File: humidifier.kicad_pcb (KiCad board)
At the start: 2 copper layers, 39 x 24 mm, 12 parts, among them J1 Level, J2 PWR, Q1 IRF740, U1 NE555

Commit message: Release candidate.
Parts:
- added D1: 4141, Diode_THT:D_DO-15_P3.81mm_Vertical_AnodeUp, B.Cu at (101.2, 88.0)
- added J3: FAN, Connector_Wire:SolderWirePad_1x02_P7.62mm_Drill2mm, F.Cu at (107.2, 100.0)
- added Q2: 13001, Package_TO_SOT_THT:TO-92, B.Cu at (96.2, 88.0)
- added R1: 1k, Resistor_SMD:R_0805_2012Metric_Pad1.15x1.40mm_HandSolder, F.Cu at (93.2, 93.0)
- RV1: footprint Connector_PinSocket_2.54mm:PinSocket_1x03_P2.54mm_Vertical -> Potentiometer_THT:Potentiometer_Bourns_3386P_Vertical
- moved Q1 127.7 mm to (71.2, 96.0), turned to 90 degrees
- moved C3 122.3 mm to (77.0, 86.2)
- moved J1 122.3 mm to (65.5, 103.0)
- moved L1 122.3 mm to (65.5, 95.5)
- moved R4 122.1 mm to (77.2, 97.0), turned to 180 degrees
- moved BZ1 121.9 mm to (82.2, 87.8)
- moved J2 119.9 mm to (100.2, 100.0)
- moved C1 118.7 mm to (91.7, 96.5)
- moved R3 118.7 mm to (87.5, 93.1)
- moved U1 118.7 mm to (87.4, 104.0)
- moved C2 118.7 mm to (91.2, 99.4)
- moved RV1 115.9 mm to (80.2, 98.0)
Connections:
- net Net-(J1-Pad2) renamed water
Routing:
- net Net-(D1-Pad1): track 0.00 -> 43.5 mm
- net VCC: track 56.2 -> 68.9 mm
- net 26: track 14.1 -> 26.7 mm
- net water: track 17.4 -> 29.3 mm
- net GND: track 59.9 -> 66.2 mm
- net Net-(Q2-Pad3): track 0.00 -> 5.22 mm
- net Net-(C3-Pad2): track 18.5 -> 14.5 mm
- net Net-(Q1-Pad1): track 3.11 -> 5.97 mm
- net Net-(BZ1-Pad1): track 5.16 -> 5.91 mm
- added copper zone on F.Cu, net VCC
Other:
- board size 39 x 24 mm -> 50 x 25 mm
- board text added: "+"
- board text added: "-"
- board text added: "BZ"
- board text added: "GND"
- board text added: "HUM-1.1"
- board text added: "L1"
- board text added: "fan"
- board text added: "vcc"
- board text added: "water"

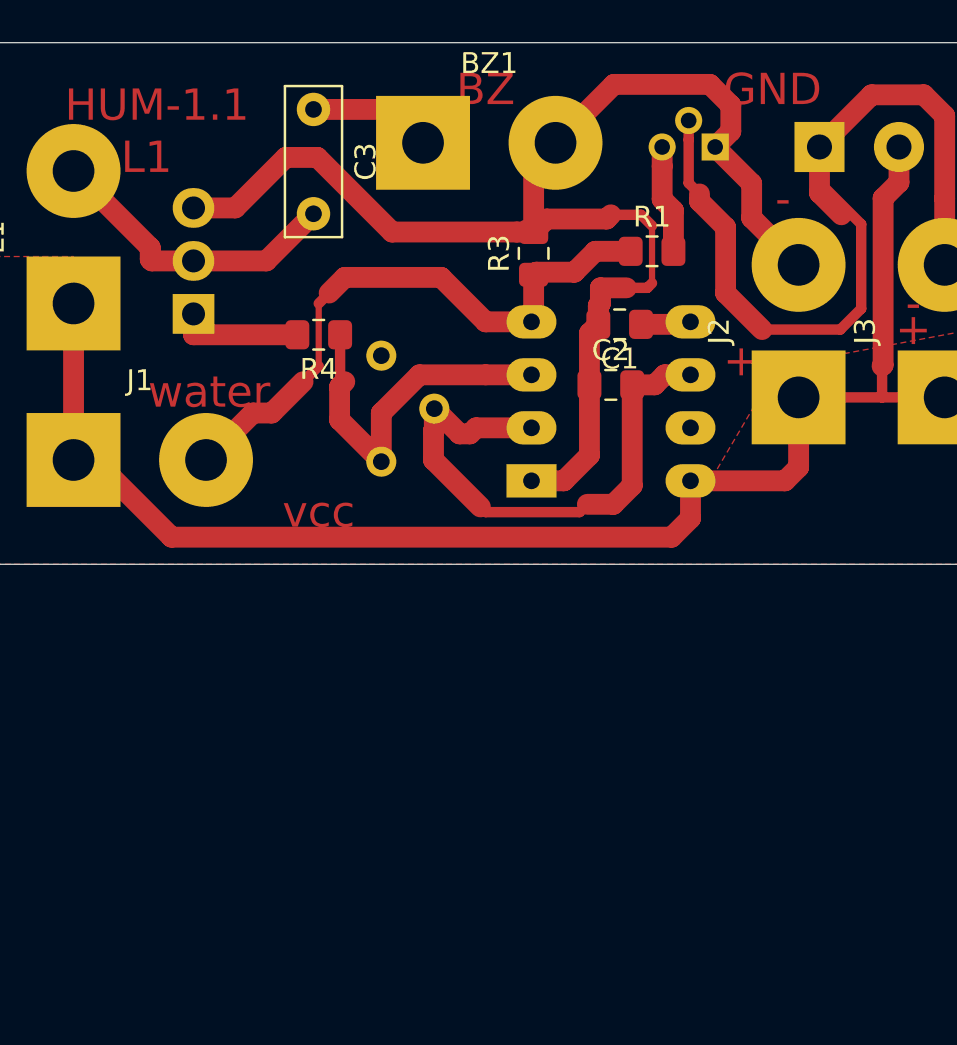
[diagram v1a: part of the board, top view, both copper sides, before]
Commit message: Added sensor based on OA lm324.
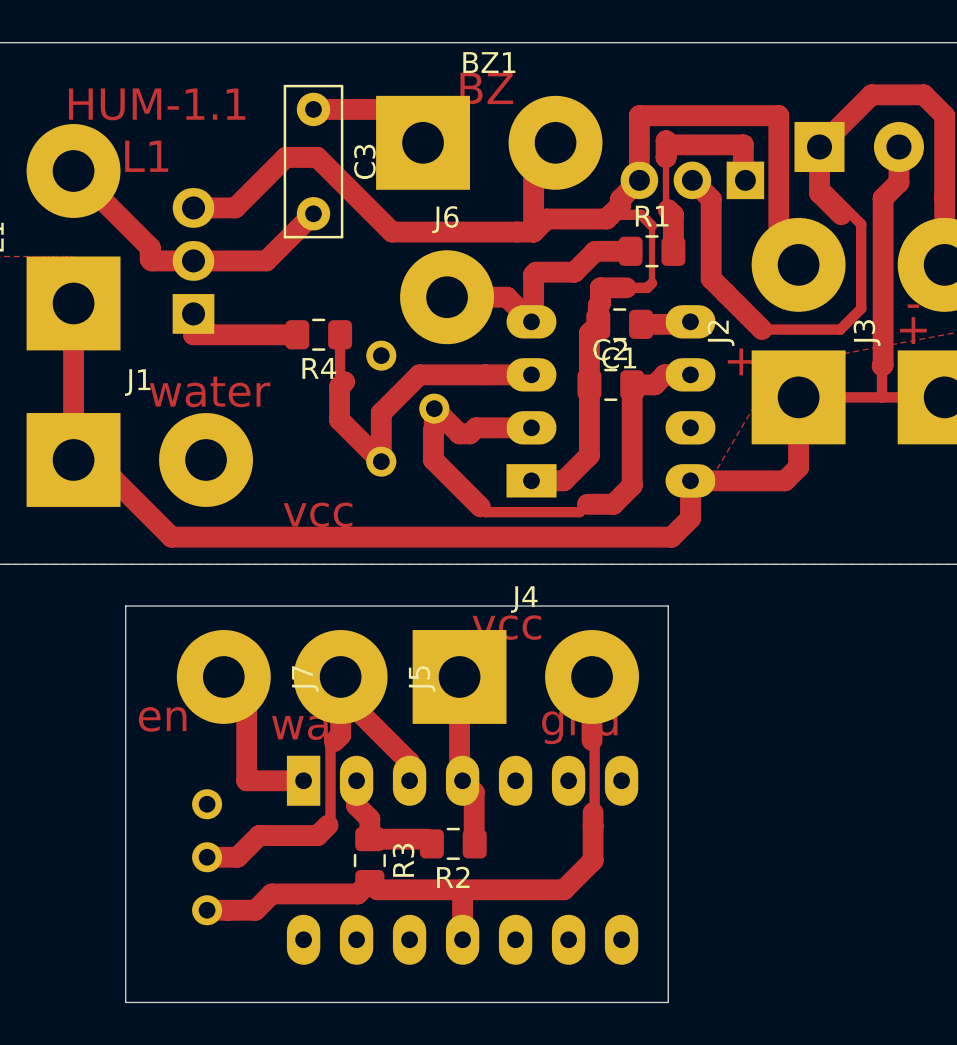
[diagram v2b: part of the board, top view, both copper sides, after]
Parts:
- added J4: PWR, Connector_Wire:SolderWirePad_1x02_P7.62mm_Drill2mm, F.Cu at (84.0, 113.4)
- added J5: water, Connector_Wire:SolderWirePad_1x01_Drill2mm, F.Cu at (78.3, 113.4)
- added J6: en, Connector_Wire:SolderWirePad_1x01_Drill2mm, F.Cu at (83.4, 95.2)
- added J7: en, Connector_Wire:SolderWirePad_1x01_Drill2mm, F.Cu at (72.7, 113.4)
- added R2: 47k, Resistor_SMD:R_0805_2012Metric_Pad1.15x1.40mm_HandSolder, F.Cu at (83.7, 121.4)
- added RV2: 100K, Potentiometer_THT:Potentiometer_Bourns_3296W_Vertical, B.Cu at (71.9, 119.5)
- added U2: LM324, Package_DIP:DIP-14_W7.62mm_LongPads, B.Cu at (76.5, 118.4)
- Q2: value 13001 -> MJE13003; footprint Package_TO_SOT_THT:TO-92 -> Package_TO_SOT_THT:TO-126-3_Vertical
- R3: value 1K -> 47K
- moved R3 30.1 mm to (79.7, 122.2), turned to 270 degrees
- moved Q2 2.16 mm to (97.7, 89.6)
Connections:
- Q2 pad 1: GND -> Net-(Q2-Pad1)
- Q2 pad 3: Net-(Q2-Pad3) -> GND
- R1 pad 1: water -> EN
- R1 pad 2: Net-(Q2-Pad3) -> Net-(Q2-Pad1)
- R3 pad 1: water -> Net-(R2-Pad2)
- U1 pad 4: water -> EN
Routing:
- net GND: track 66.2 -> 98.0 mm
- net EN: track 0.00 -> 20.1 mm
- net Net-(Q2-Pad1): track 0.00 -> 11.0 mm
- net VCC: track 68.9 -> 77.2 mm
- net water: track 29.3 -> 22.2 mm
- net Net-(R2-Pad2): track 0.00 -> 6.13 mm
- net Net-(Q2-Pad3): track 5.22 -> 0.00 mm
- net Net-(D1-Pad1): track 43.5 -> 40.6 mm
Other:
- board size 50 x 25 mm -> 50 x 46 mm
- board text added: "en"
- board text added: "gnd"
- board text added: "wa"
- board text removed: "GND"

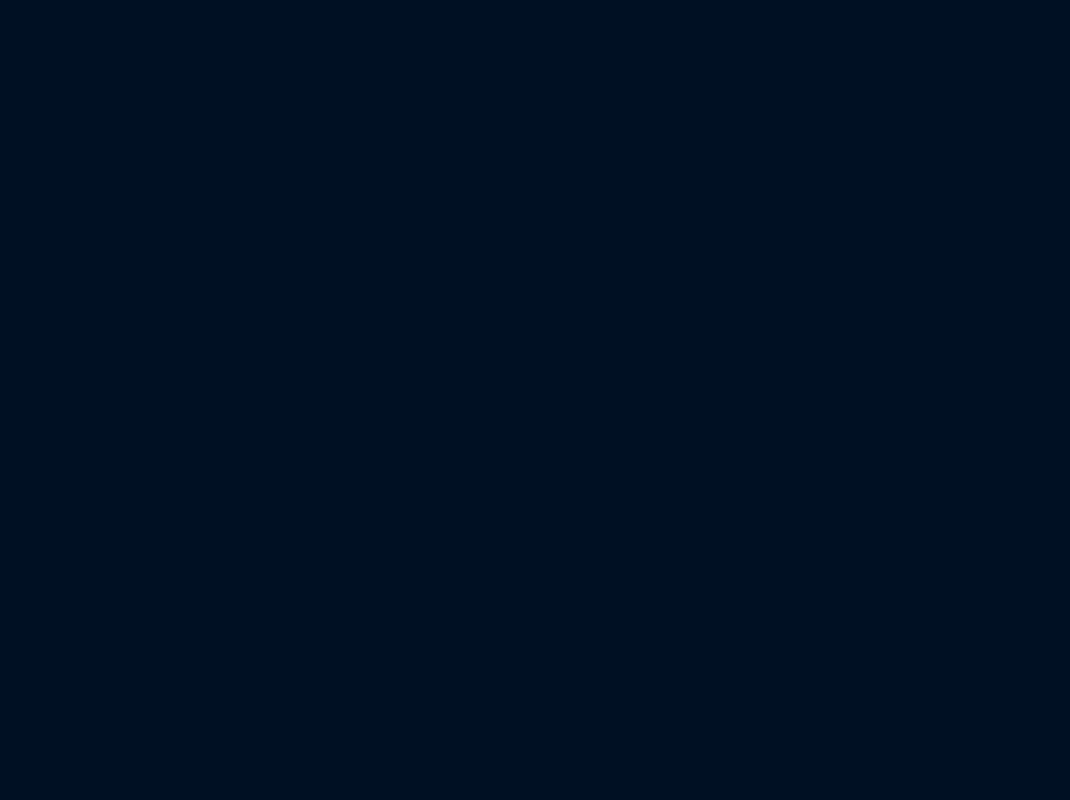
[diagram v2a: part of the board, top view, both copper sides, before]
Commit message: Added timer.
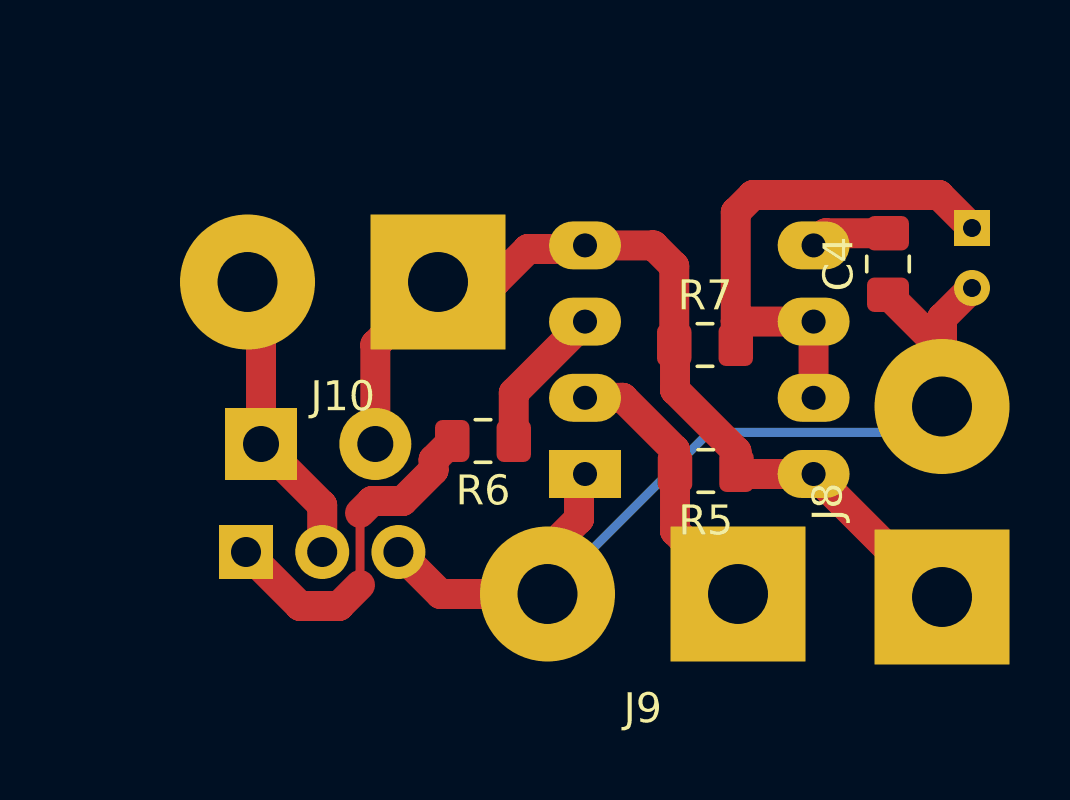
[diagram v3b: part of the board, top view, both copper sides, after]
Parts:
- added C4: 100n, Capacitor_SMD:C_0805_2012Metric_Pad1.15x1.40mm_HandSolder, F.Cu at (124.4, 119.4)
- added C5: 10u, Capacitor_THT:CP_Radial_D4.0mm_P2.00mm, B.Cu at (127.2, 118.2)
- added D2: 4141, Diode_THT:D_DO-15_P3.81mm_Vertical_AnodeUp, B.Cu at (103.5, 125.4)
- added J10: REL, Connector_Wire:SolderWirePad_1x02_P7.62mm_Drill2mm, F.Cu at (109.4, 120.0)
- added J8: PWR, Connector_Wire:SolderWirePad_1x02_P7.62mm_Drill2mm, F.Cu at (126.2, 130.5)
- added J9: THNX, Connector_Wire:SolderWirePad_1x02_P7.62mm_Drill2mm, F.Cu at (119.4, 130.4)
- added Q3: MJE13003, Package_TO_SOT_THT:TO-126-3_Vertical, B.Cu at (103.0, 129.0)
- added R5: 100K, Resistor_SMD:R_0805_2012Metric_Pad1.15x1.40mm_HandSolder, F.Cu at (118.3, 126.3)
- added R6: 1k, Resistor_SMD:R_0805_2012Metric_Pad1.15x1.40mm_HandSolder, F.Cu at (110.9, 125.3)
- added R7: 500K, Resistor_SMD:R_0805_2012Metric_Pad1.15x1.40mm_HandSolder, F.Cu at (118.3, 122.1)
- added U3: NE555, Package_DIP:DIP-8_W7.62mm_LongPads, B.Cu at (114.3, 126.4)
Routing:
- net GND: track 98.0 -> 132.6 mm
- net VCC: track 77.2 -> 108.4 mm
- net Net-(C5-Pad1): track 0.00 -> 18.1 mm
- net Net-(Q3-Pad1): track 0.00 -> 11.5 mm
- net REL: track 0.00 -> 10.0 mm
- net Net-(J9-Pad1): track 0.00 -> 9.39 mm
- net Net-(R6-Pad1): track 0.00 -> 4.96 mm
- net Net-(C4-Pad2): track 0.00 -> 2.65 mm

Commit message: Added annotations.
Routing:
- net Net-(Q3-Pad1): track 11.5 -> 12.5 mm
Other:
- board size 50 x 46 mm -> 69.8 x 51 mm
- board text added: "pwr"
- board text added: "rel"
- board text added: "txh"
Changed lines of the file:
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@@
   (general
     (thickness 1.6)
-    (drawings 23)
+    (drawings 31)
     (tracks 227)
     (zones 0)
@@
   )
   (setup
-    (last_trace_width 0.3)
+    (last_trace_width 0.25)
     (user_trace_width 0.3)
     (user_trace_width 0.5)
@@
     (add_net "Net-(R4-Pad1)")
     (add_net "Net-(R6-Pad1)")
-    (add_net "Net-(RV1-Pad1)")
-    (add_net "Net-(RV2-Pad1)")
-    (add_net "Net-(U1-Pad7)")
     (add_net REL)
     (add_net VCC)
@@
       (net 2 "Net-(BZ1-Pad1)"))
   )
+  (gr_text rel (at 104.9 117.7) (layer F.Cu)
+    (effects (font (size 1.5 1.5) (thickness 0.3)))
+  )
+  (gr_text + (at 124 127.1) (layer F.Cu)
+    (effects (font (size 1.5 1.5) (thickness 0.3)))
+  )
+  (gr_text "pwr\n" (at 126.9 127.5) (layer F.Cu)
+    (effects (font (size 1.5 1.5) (thickness 0.3)))
+  )
+  (gr_text txh (at 110 132) (layer F.Cu)
+    (effects (font (size 1.5 1.5) (thickness 0.3)))
+  )
+  (gr_line (start 131 116) (end 99 116) (layer Edge.Cuts) (width 0.05))
+  (gr_line (start 131 134) (end 131 116) (layer Edge.Cuts) (width 0.05))
+  (gr_line (start 99 134) (end 131 134) (layer Edge.Cuts) (width 0.05))
+  (gr_line (start 99 116) (end 99 134) (layer Edge.Cuts) (width 0.05))
   (gr_text gnd (at 89.8 115.5) (layer F.Cu)
     (effects (font (size 1.5 1.5) (thickness 0.3)))
@@
   (segment (start 117.3 126.3) (end 117.3 125.6) (width 1) (layer F.Cu) (net 17))
   (segment (start 117.3 125.6) (end 115.56 123.86) (width 1) (layer F.Cu) (net 17))
-  (segment (start 108.222001 127.300001) (end 107.199999 127.300001) (width 1) (layer F.Cu) (net 18))
-  (segment (start 109.251628 126.270374) (end 108.222001 127.300001) (width 1) (layer F.Cu) (net 18))
-  (segment (start 109.875 125.3) (end 109.251628 125.923372) (width 1) (layer F.Cu) (net 18))
-  (segment (start 109.251628 125.923372) (end 109.251628 126.270374) (width 1) (layer F.Cu) (net 18))
-  (segment (start 107.199999 127.300001) (end 106.8 127.7) (width 1) (layer F.Cu) (net 18))
   (segment (start 103 129) (end 104.8 130.8) (width 1) (layer F.Cu) (net 18))
   (segment (start 104.8 130.8) (end 106.1 130.8) (width 1) (layer F.Cu) (net 18))
   (segment (start 106.1 130.8) (end 106.8 130.1) (width 1) (layer F.Cu) (net 18))
   (segment (start 106.8 127.7) (end 106.8 130.1) (width 0.3) (layer F.Cu) (net 18))
+  (segment (start 109.699999 127.300001) (end 107.199999 127.300001) (width 1) (layer F.Cu) (net 18))
+  (segment (start 110 127) (end 109.699999 127.300001) (width 1) (layer F.Cu) (net 18))
+  (segment (start 109.875 125.3) (end 109.875 126.875) (width 1) (layer F.Cu) (net 18))
+  (segment (start 107.199999 127.300001) (end 106.8 127.7) (width 1) (layer F.Cu) (net 18))
+  (segment (start 109.875 126.875) (end 110 127) (width 1) (layer F.Cu) (net 18))
   (segment (start 111.925 123.695) (end 111.925 125.3) (width 1) (layer F.Cu) (net 19))
   (segment (start 114.3 121.32) (end 111.925 123.695) (width 1) (layer F.Cu) (net 19))
